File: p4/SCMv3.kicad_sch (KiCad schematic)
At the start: 126 parts, among them IC1 40106, IC2 40106, IC3 TL082, J1 Conn_01x06, J1-OUT8 JACK-MONO-SWB, J2 Conn_01x02, J2-OUT7 JACK-MONO-SWB, J3 POWER, J3-OUT6 JACK-MONO-SWB, J4 Conn_01x02, J4-OUT5 JACK-MONO-SWB, J5-OUT4 JACK-MONO-SWB, J6-OUT3 JACK-MONO-SWB, J7-OUT2 JACK-MONO-SWB, J8-OUT1 JACK-MONO-SWB, J9-CLK_IN1 JCLK_IN, Q1 Si2318, Q2 Si2318, Q3 Si2318, Q4 Si2318, U1 STM32F030K6Tx, U2 AP7384-33, Y1 16MHz_18pF_FA238

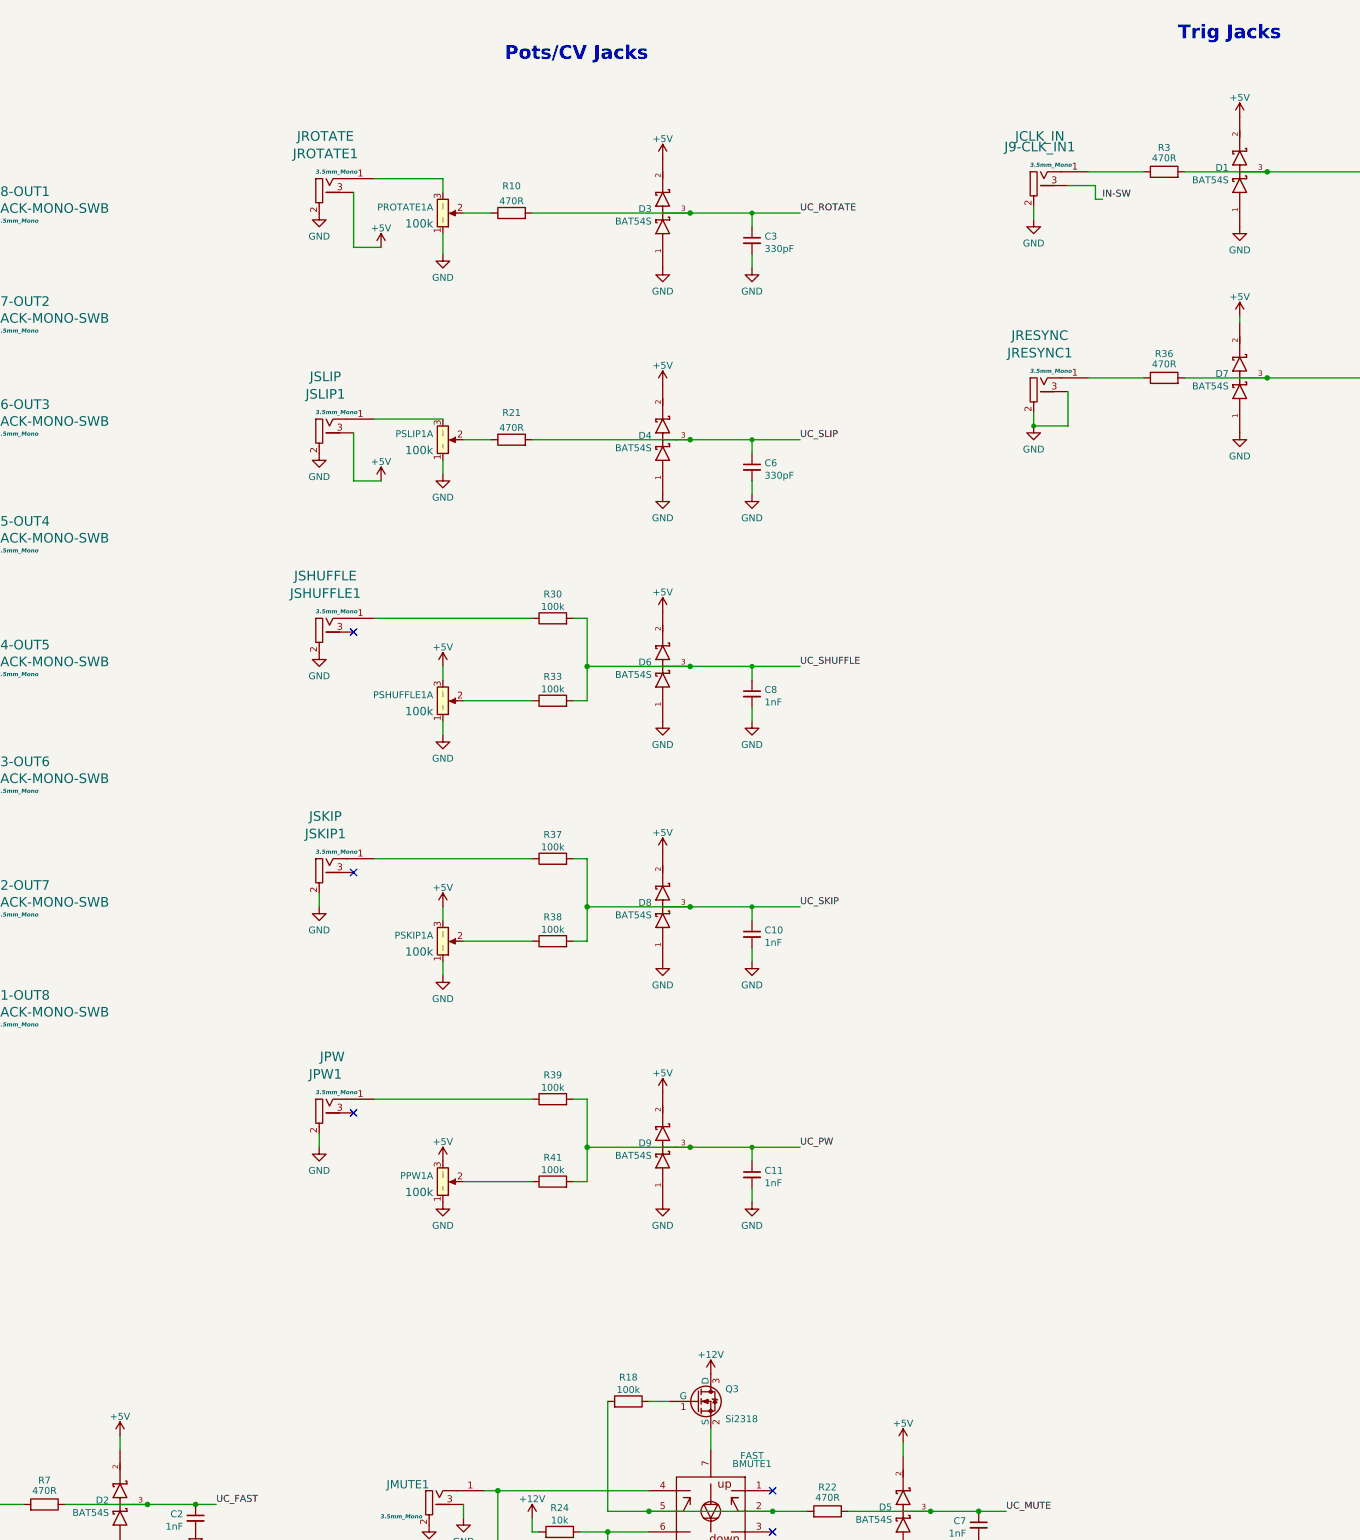
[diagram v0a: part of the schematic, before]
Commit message: changed +5V net over to +3.3VA
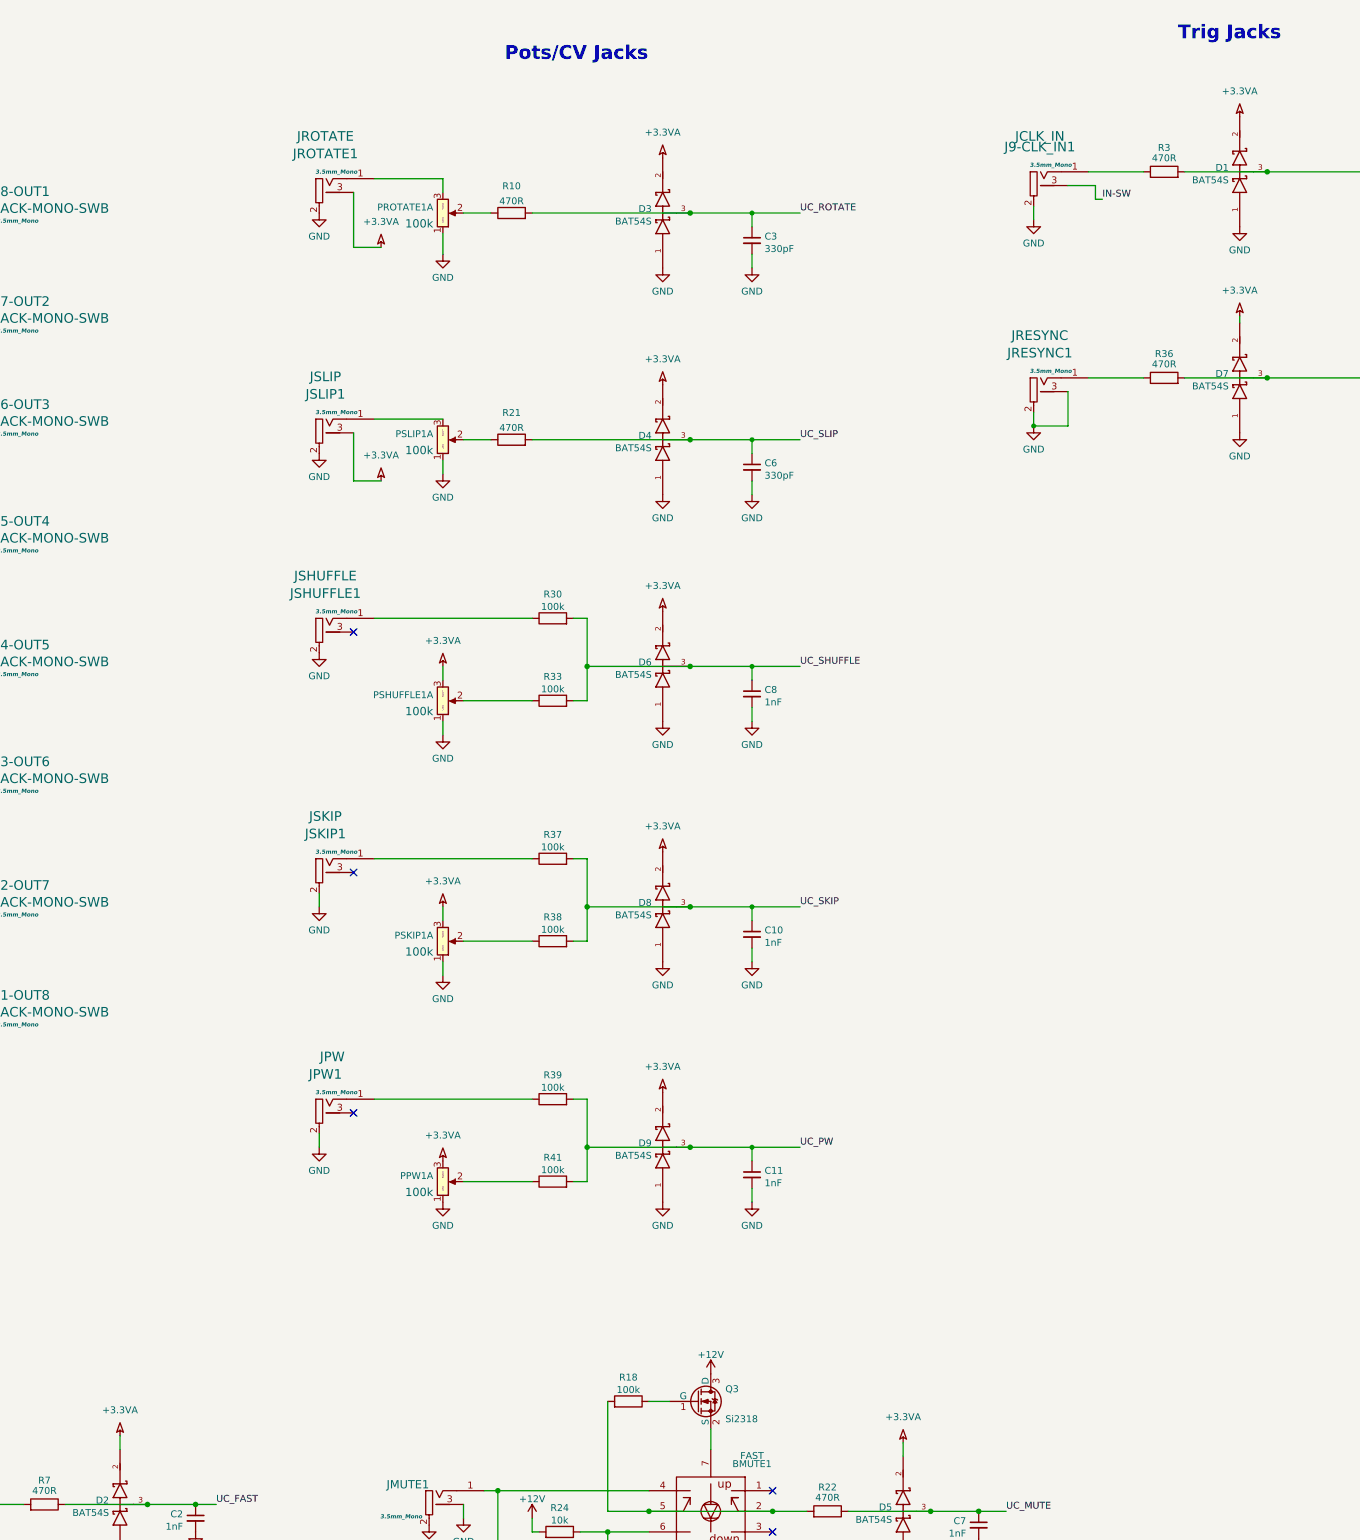
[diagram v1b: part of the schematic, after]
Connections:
- net +5V is gone; now on net +3.3VA: D1.2 (cathode), D2.2 (cathode), D3.2 (cathode), D4.2 (cathode), D5.2 (cathode), D6.2 (cathode), D7.2 (cathode), D8.2 (cathode), D9.2 (cathode), JROTATE1.3 (SW), JSLIP1.3 (SW), PPW1.3 (Right), PSHUFFLE1.3 (Right), PSKIP1.3 (Right)

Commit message: updated p4 schematic to use level shifters instead of hex inverters
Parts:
- removed C12: 47uF_5x5.3_16V, 4ms_Capacitor:CP_Elec_5x5.3, symbol 4ms_Capacitor:47uF_5x5.3_16V
- removed IC1, IC2: 40106, 4ms_Package_SSOP:TSSOP-14_4.4x5mm_P0.65mm, symbol 4ms_IC:CD40106BPWR
- removed VR2: UA78L08, 4ms_Package_SOT:SOT89-3, symbol 4ms_Regulator:UA78L08
- added C12: 0.1uF_0603_16V, 4ms_Capacitor:C_0603, symbol 4ms_Capacitor:0.1uF_0603_16V
- added U3, U4: CD40109BPWR, Package_SO:TSSOP-16_4.4x5mm_P0.65mm, symbol 4ms_IC:CD40109BPWR
- BFAST1, BMUTE1: Display FAST -> Orange Button
- C15, C16, C17, C18, C19, C20, C22, C23, C24: JLCPCB ID C14663 -> (none); Manufacturer AVX Corporation -> (none); Part Number 0603YC104KAT2A -> (none)
- D1, D2, D3, D4, D5, D6, D7, D8, D9: Alt JLCPCB ID (none) -> C122856
- J1-OUT8, J2-OUT7, J3-OUT6, J4-OUT5, J5-OUT4, J6-OUT3, J7-OUT2, J8-OUT1: value JACK-MONO-SWB -> 3.5mm_Mono_Switched_SymSmall_0.05
- J3: value POWER -> Conn_02x08
- J9-CLK_IN1: value JCLK_IN -> 3.5mm_Mono_Switched_SymSmall_0.05
- JFAST1, JMUTE1: value 3.5mm_Stereo_SymSmall_0.05 -> 3.5mm_Mono_Switched_SymSmall_0.05
- JPW1: value JPW -> 3.5mm_Mono_Switched_SymSmall_0.05
- JRESYNC1: value JRESYNC -> 3.5mm_Mono_Switched_SymSmall_0.05
- JROTATE1: value JROTATE -> 3.5mm_Mono_Switched_SymSmall_0.05
- JSHUFFLE1: value JSHUFFLE -> 3.5mm_Mono_Switched_SymSmall_0.05
- JSKIP1: value JSKIP -> 3.5mm_Mono_Switched_SymSmall_0.05
- JSLIP1: value JSLIP -> 3.5mm_Mono_Switched_SymSmall_0.05
- LED1, LED7, LED8: value BLUE -> RGB_CA_PLCC4
- LED2, LED3, LED4, LED5, LED6: value GREEN -> RGB_CA_PLCC4
- LED9: value WHITE -> RGB_CA_PLCC4
- R10, R13, R21, R22, R27, R3, R36, R7: value 470R_0805_350mW -> 470R_0603
- U2: value AP7384-33 -> (none); footprint 4ms_Package_SOT:SOT23-3_PO132 -> (none)
- VR1: value LD1117S33 -> (none); Datasheet 2 https://www.mouser.com/datasheet/2/115/DIOD_S_A0007713706_1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 -> (none); Display 3.3V 150mA -> (none); Manufacturer 2 Diodes Inc. -> (none); Part Number 2 AZ1117IH-3.3TRG1 -> (none); Specifications LDO 3.3V, Vin(min)>12V, Iout(max, no HS)>150mA -> (none)
- Y1: JLCPCB ID C90906 -> C90906 (12pF)
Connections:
- net +12V: now also C20.1, U3.16 (Vdd), U4.16 (Vdd)
- net +3.3VA: no longer D1.2 (cathode), D3.2 (cathode), D4.2 (cathode), D5.2 (cathode), D6.2 (cathode), D7.2 (cathode), D8.2 (cathode), D9.2 (cathode)
- net +3V3: now also C17.1, D1.2 (cathode), D3.2 (cathode), D4.2 (cathode), D5.2 (cathode), D6.2 (cathode), D7.2 (cathode), D8.2 (cathode), D9.2 (cathode), R42.1, C12.1, U3.1 (Vcc), U3.15 (EN), U3.2 (EN), U3.7 (EN), U3.9 (EN), U4.1 (Vcc), U4.15 (EN), U4.2 (EN), U4.7 (EN), U4.9 (EN); no longer TRIM1.3 (Right)
- net GND: now also TRIM1.1 (Left), C12.2, U3.8 (GND), U4.8 (GND); no longer R42.2
- net UC_LED_IN: now also LED9.2 (A); no longer R1.1, R2.1, R4.1
- net UC_OUT1: now also LED8.2 (A), U3.3 (In); no longer R8.1
- net UC_OUT2: now also LED7.2 (A), U3.6 (In); no longer R14.1
- net UC_OUT3: now also LED6.2 (A), U3.10 (In); no longer R17.1
- net UC_OUT4: now also LED5.2 (A), U3.14 (In); no longer R20.1
- net UC_OUT5: now also LED4.2 (A), U4.3 (In); no longer R25.1
- net UC_OUT6: now also LED3.2 (A), U4.6 (In); no longer R29.1
- net UC_OUT7: now also LED2.2 (A), U4.10 (In); no longer R32.1
- net UC_OUT8: now also LED1.2 (A), U4.14 (In); no longer R35.1
- net at R12.1: now also U3.5 (Out)
- net at R28.1: now also U4.5 (Out)
- net at R34.1: now also U4.13 (Out)
- net at R31.1: now also U4.11 (Out)
- net at R6.1: now also U3.4 (Out)
- net at R23.1: now also U4.4 (Out)
- net at R15.1: now also U3.11 (Out)
- net at R19.1: now also U3.13 (Out)
- removed net +8V: C17.1, C20.1
- removed net VREF: IC3.1, IC3.2 (-), LED1.2 (A), LED2.2 (A), LED3.2 (A), LED4.2 (A), LED5.2 (A), LED6.2 (A), LED7.2 (A), LED8.2 (A), LED9.2 (A)
- new net: R42.2, TRIM1.3 (Right)
- new net VLEDSINK: IC3.1, IC3.2 (-), R1.1, R14.1, R17.1, R2.1, R20.1, R25.1, R29.1, R32.1, R35.1, R4.1, R8.1
- no-connect marks 42 -> 38
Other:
- note removed: "Outputs"
- note removed: "Unused gates"
- moved on the sheet: C14, C16, C18, C19, C21, C22, C23, IC3A, IC3C, LED1, LED2, LED3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

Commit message: WIP updating p4
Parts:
- R1: value 4.7k_0603 -> 2.7k_0603; symbol 4ms_Resistor:4.7k_0603 -> 4ms_Resistor:2.7k_0603; Display 4.7k -> 2.7k; JLCPCB ID C23162 -> C13167; Part Number RC0603FR-074K7L -> RC0603FR-072K7L; Specifications 4k7, 1%, 1/10W, 0603 -> 2k7, 1%, 1/10W, 0603
- R14, R35, R8: value 4.7k_0603 -> 1k_0603; symbol 4ms_Resistor:4.7k_0603 -> 4ms_Resistor:1k_0603; Display 4.7k -> 1k; JLCPCB ID C23162 -> C21190; Part Number RC0603FR-074K7L -> RC0603FR-071KL; Specifications 4k7, 1%, 1/10W, 0603 -> 1K, 1%, 1/10W, 0603
- R22: value 470R_0603 -> 4.7k_0603; symbol 4ms_Resistor:470R_0603 -> 4ms_Resistor:4.7k_0603; Display 470R -> 4.7k; JLCPCB ID C23179 -> C23162; Part Number RC0603FR-07470RL -> RC0603FR-074K7L; Specifications 470R, 1%, 1/10W, 0603 -> 4k7, 1%, 1/10W, 0603
- R7: symbol 4ms_Resistor:470R_0603 -> 4ms_Resistor:4.7k_0603; Display 470R -> 4.7k; JLCPCB ID C23179 -> C23162; Part Number RC0603FR-07470RL -> RC0603FR-074K7L; Specifications 470R, 1%, 1/10W, 0603 -> 4k7, 1%, 1/10W, 0603
- U2: value (none) -> AP7384-33; footprint (none) -> 4ms_Package_SOT:SOT23-3_PO132
- VR1: value (none) -> LD1117-3.3V-SOT223
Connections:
- net +3.3VA: no longer D2.2 (cathode)
- net +3V3: now also D2.2 (cathode)
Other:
- note added: "Changes: -R7/R22 bigger, less taxing on D2/D5 -use level shifter not inverter -LEDs reversed -LED resistors tweaked (brighter blues, redder white)"
- note added: "TODO: Use ref for Va? Pot/CV redo: -all attenuator or all offset? -offset: need to go full range with pot when jack is patched -need lower impedance into uC: opamp or lower resistors"
